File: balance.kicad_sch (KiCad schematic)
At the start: 30 parts, among them Q10 2N7002, Q5 AO3401A, Q6 AO3401A, Q7 AO3401A, Q8 2N7002, Q9 2N7002

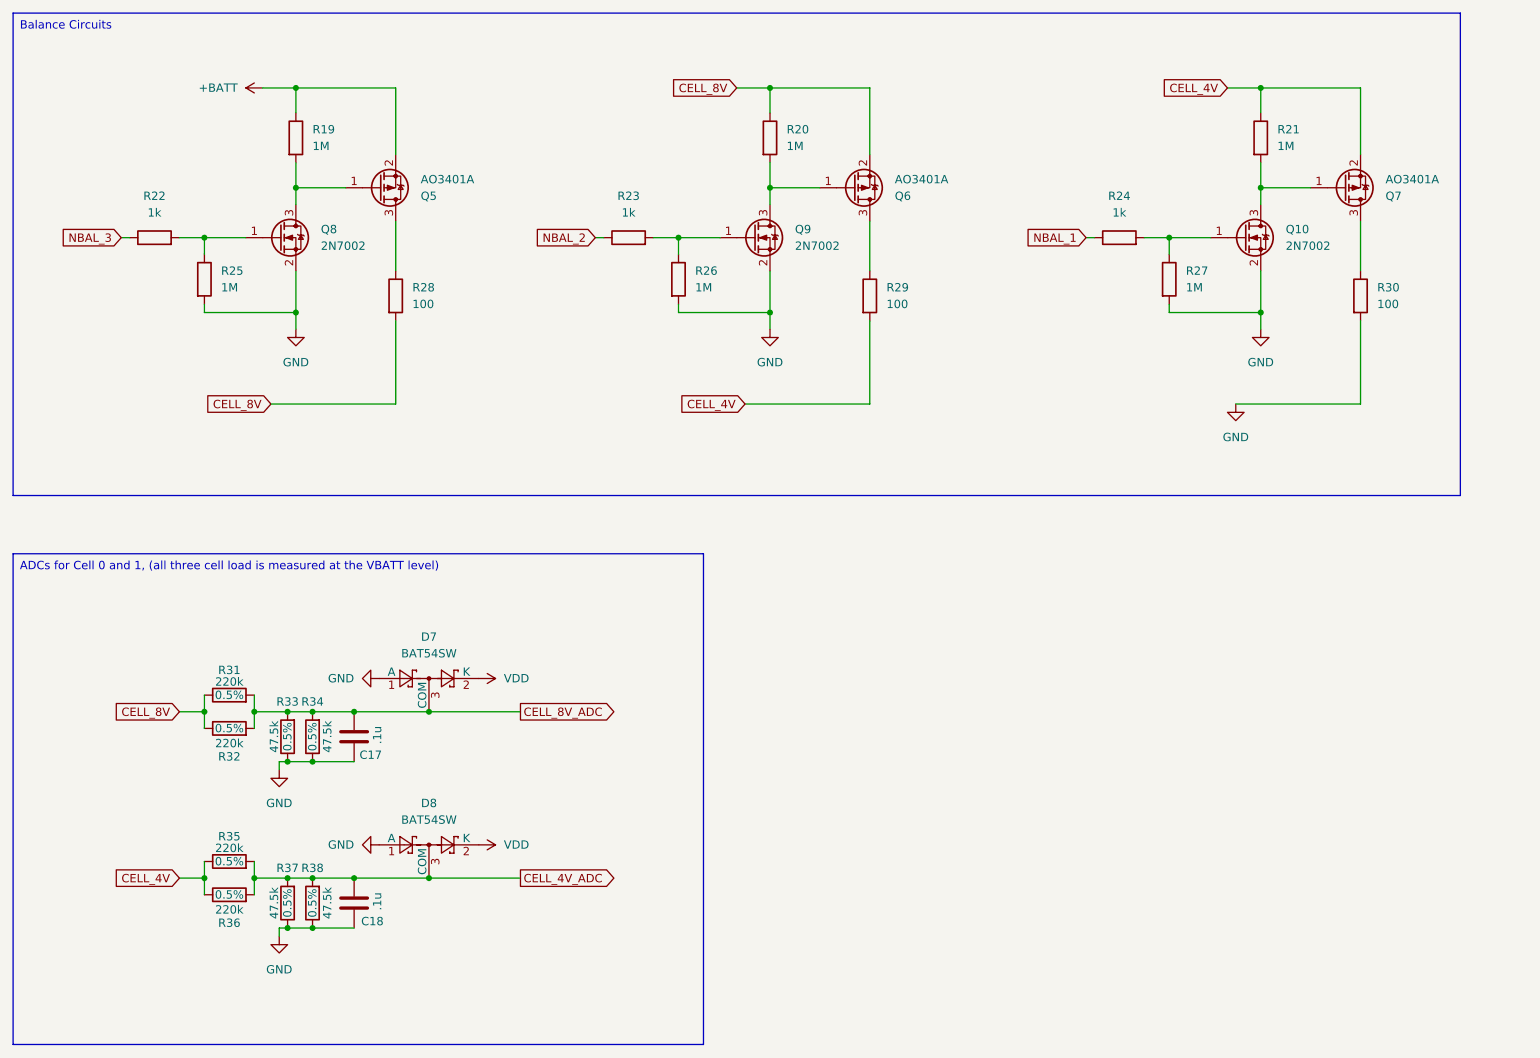
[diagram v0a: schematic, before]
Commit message: Adding flow chart to main.c Adding leds on balancers
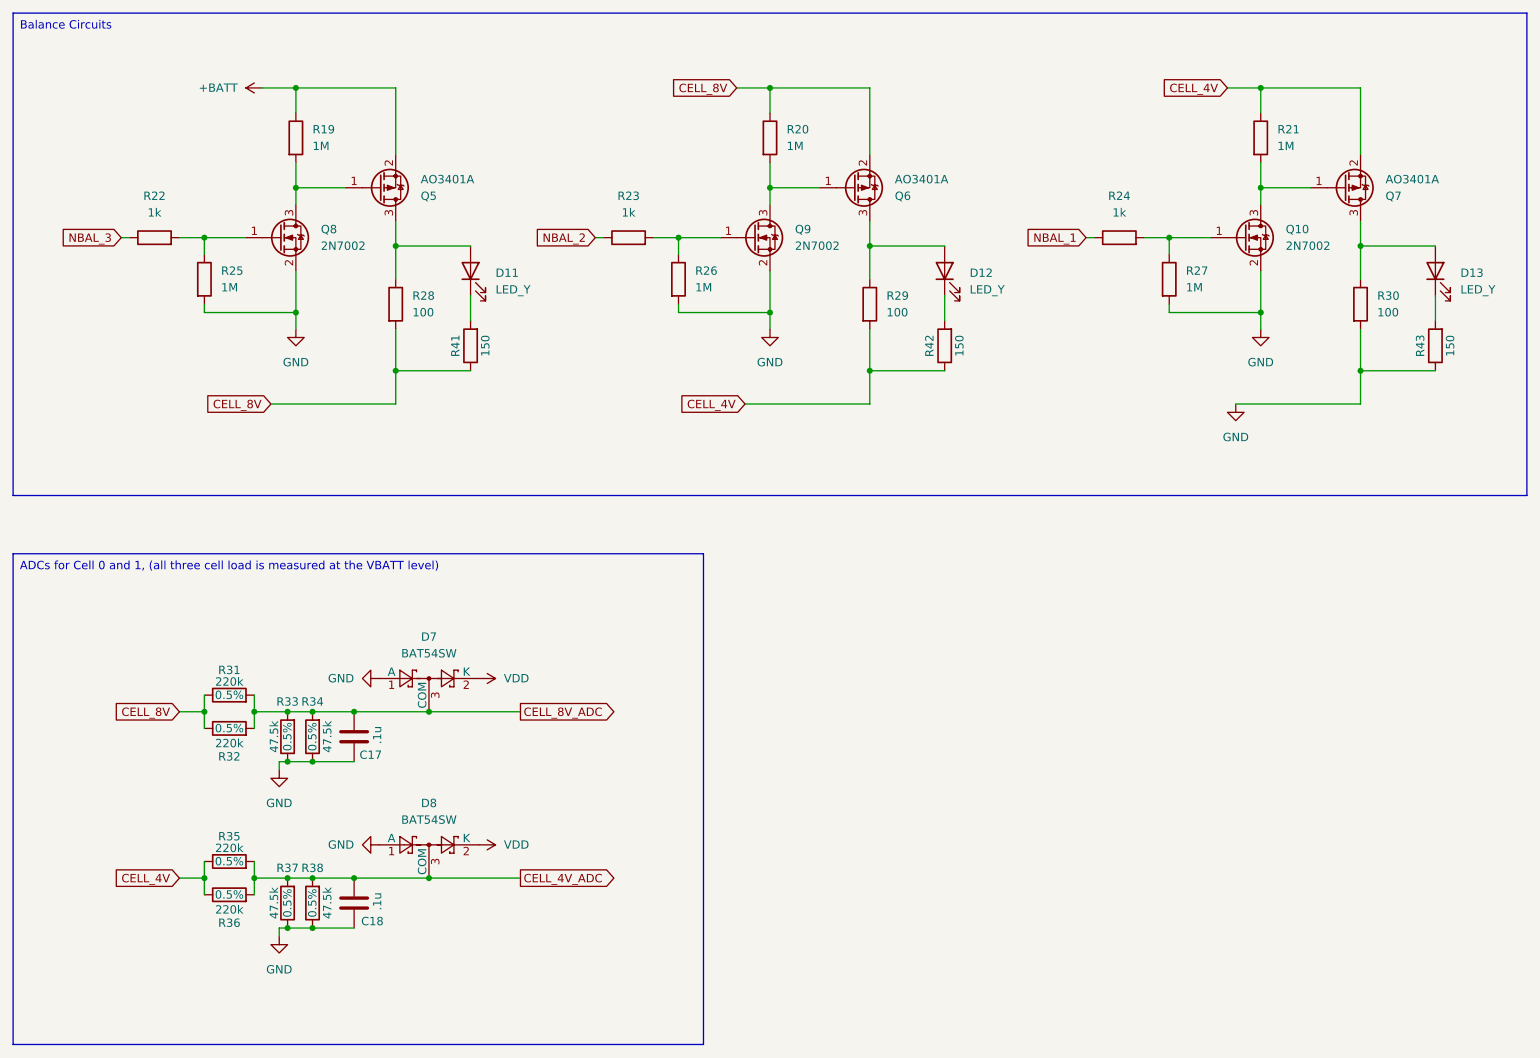
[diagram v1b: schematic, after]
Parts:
- added D11, D12, D13: LED_Y, LED_SMD:LED_0603_1608Metric, symbol Device:LED
- added R41, R42, R43: 150, Resistor_SMD:R_0402_1005Metric, symbol Device:R
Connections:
- net CELL_4V: now also R42.1
- net CELL_8V: now also R41.1
- net GND: now also R43.1
- net at Q7.3 (D), R30.1: now also D13.2 (A)
- net at Q6.3 (D), R29.1: now also D12.2 (A)
- net at Q5.3 (D), R28.1: now also D11.2 (A)
- new net: D12.1 (K), R42.2
- new net: D13.1 (K), R43.2
- new net: D11.1 (K), R41.2
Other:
- moved on the sheet: R28, R29, R30

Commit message: Starting draft of ADC multiplexer
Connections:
- net CELL_4V: no longer R35.1, R36.1
- net CELL_8V: no longer R31.1, R32.1
- net CELL_4V_ADC: no longer names the net of C18.1, D8.3 (COM), R35.2, R36.2, R37.2, R38.2
- net CELL_8V_ADC: no longer names the net of C17.1, D7.3 (COM), R31.2, R32.2, R33.2, R34.2
- new net: R31.1, R32.1
- new net: R35.1, R36.1
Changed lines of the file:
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@@
-		)
-	)
-	(global_label "CELL_4V"
-		(shape input)
-		(at 63.5 157.48 180)
-		(fields_autoplaced yes)
-		(effects
-			(font
-				(size 1.27 1.27)
-			)
-			(justify right)
-		)
-		(property "Intersheetrefs" "${INTERSHEET_REFS}"
-			(at 52.7739 157.48 0)
-			(effects
-				(font
-					(size 1.27 1.27)
-				)
-				(justify right)
-				(hide yes)
-			)
 		)
 	)
@@
 				)
 				(justify right)
-				(hide yes)
-			)
-		)
-	)
-	(global_label "CELL_4V_ADC"
-		(shape output)
-		(at 115.57 157.48 0)
-		(fields_autoplaced yes)
-		(effects
-			(font
-				(size 1.27 1.27)
-			)
-			(justify left)
-		)
-		(property "Intersheetrefs" "${INTERSHEET_REFS}"
-			(at 130.8923 157.48 0)
-			(effects
-				(font
-					(size 1.27 1.27)
-				)
-				(justify left)
 				(hide yes)
 			)
@@
 				(hide yes)
 			)
-		)
-	)
-	(global_label "CELL_8V"
-		(shape input)
-		(at 63.5 132.08 180)
-		(fields_autoplaced yes)
-		(effects
-			(font
-				(size 1.27 1.27)
-			)
-			(justify right)
-		)
-		(property "Intersheetrefs" "${INTERSHEET_REFS}"
-			(at 52.7739 132.08 0)
-			(effects
-				(font
-					(size 1.27 1.27)
-				)
-				(justify right)
-				(hide yes)
-			)
-		)
-	)
-	(global_label "CELL_8V_ADC"
-		(shape output)
-		(at 115.57 132.08 0)
-		(fields_autoplaced yes)
-		(effects
-			(font
-				(size 1.27 1.27)
-			)
-			(justify left)
-		)
-		(property "Intersheetrefs" "${INTERSHEET_REFS}"
-			(at 130.8923 132.08 0)
-			(effects
-				(font
-					(size 1.27 1.27)
-				)
-				(justify left)
-				(hide yes)
-			)

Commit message: Adding ADC multiplexer, protection diodes
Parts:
- removed C17, C18: .1u, Capacitor_SMD:C_0603_1608Metric, symbol Device:C
- removed D7, D8: BAT54SW, Package_TO_SOT_SMD:SOT-323_SC-70, symbol Diode:BAT54SW
- removed R31, R32, R35, R36: 220k, Resistor_SMD:R_0402_1005Metric, symbol Device:R
- removed R33, R34, R37, R38: 47.5k, Resistor_SMD:R_0402_1005Metric, symbol Device:R

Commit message: Decent pass
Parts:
- renumbered D11 to D13, D12 to D14, D13 to D15, Q6 to Q10, Q10 to Q11, Q7 to Q12, Q8 to Q7, Q5 to Q8, R22 to R25, R25 to R26, R19 to R27, R41 to R29, R23 to R30, R26 to R31, R20 to R32, R29 to R33, R42 to R34, R24 to R35, R27 to R36, R21 to R37, R30 to R38, R43 to R39
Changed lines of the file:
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@@
 		(dnp no)
 		(fields_autoplaced yes)
-		(property "Reference" "D12"
+		(property "Reference" "D14"
 			(at 184.15 65.0874 90)
 			(effects
@@
 			(project "JPBms2"
 				(path "/d86e471c-a8be-422d-a5d1-5a4699b7b766/220685a5-608c-4c12-9441-6825efcef07c"
-					(reference "D12")
+					(reference "D14")
 					(unit 1)
 				)
@@
 		(dnp no)
 		(fields_autoplaced yes)
-		(property "Reference" "#PWR042"
+		(property "Reference" "#PWR048"
 			(at 80.01 36.83 0)
 			(effects
@@
 			(project "JPBms2"
 				(path "/d86e471c-a8be-422d-a5d1-5a4699b7b766/220685a5-608c-4c12-9441-6825efcef07c"
-					(reference "#PWR042")
+					(reference "#PWR048")
 					(unit 1)
 				)
@@
 		(dnp no)
 		(fields_autoplaced yes)
-		(property "Reference" "R25"
+		(property "Reference" "R26"
 			(at 69.85 64.7699 0)
 			(effects
@@
 			(project "JPBms2"
 				(path "/d86e471c-a8be-422d-a5d1-5a4699b7b766/220685a5-608c-4c12-9441-6825efcef07c"
-					(reference "R25")
+					(reference "R26")
 					(unit 1)
 				)
@@
 		(dnp no)
 		(fields_autoplaced yes)
-		(property "Reference" "R27"
+		(property "Reference" "R36"
 			(at 217.17 64.7699 0)
 			(effects
@@
 			(project "JPBms2"
 				(path "/d86e471c-a8be-422d-a5d1-5a4699b7b766/220685a5-608c-4c12-9441-6825efcef07c"
-					(reference "R27")
+					(reference "R36")
 					(unit 1)
 				)
@@
 		(dnp no)
 		(fields_autoplaced yes)
-		(property "Reference" "R24"
+		(property "Reference" "R35"
 			(at 207.01 53.34 90)
 			(effects
@@
 			(project "JPBms2"
 				(path "/d86e471c-a8be-422d-a5d1-5a4699b7b766/220685a5-608c-4c12-9441-6825efcef07c"
-					(reference "R24")
+					(reference "R35")
 					(unit 1)
 				)
@@
 		(on_board yes)
 		(dnp no)
-		(property "Reference" "R42"
+		(property "Reference" "R34"
 			(at 178.054 76.2 90)
 			(effects
@@
 			(project "JPBms2"
 				(path "/d86e471c-a8be-422d-a5d1-5a4699b7b766/220685a5-608c-4c12-9441-6825efcef07c"
-					(reference "R42")
+					(reference "R34")
 					(unit 1)
 				)
@@
 		(on_board yes)
 		(dnp no)
-		(property "Reference" "R43"
+		(property "Reference" "R39"
 			(at 252.984 76.2 90)
 			(effects
@@
 			(project "JPBms2"
 				(path "/d86e471c-a8be-422d-a5d1-5a4699b7b766/220685a5-608c-4c12-9441-6825efcef07c"
-					(reference "R43")
+					(reference "R39")
 					(unit 1)
 				)
@@
 		(dnp no)
 		(fields_autoplaced yes)
-		(property "Reference" "Q8"
+		(property "Reference" "Q7"
 			(at 85.09 58.4199 0)
 			(effects
@@
 			(project "JPBms2"
 				(path "/d86e471c-a8be-422d-a5d1-5a4699b7b766/220685a5-608c-4c12-9441-6825efcef07c"
-					(reference "Q8")
+					(reference "Q7")
 					(unit 1)
 				)
@@
 		(dnp no)
 		(fields_autoplaced yes)
-		(property "Reference" "R26"
+		(property "Reference" "R31"
 			(at 142.24 64.7699 0)
 			(effects
@@
 			(project "JPBms2"
 				(path "/d86e471c-a8be-422d-a5d1-5a4699b7b766/220685a5-608c-4c12-9441-6825efcef07c"
-					(reference "R26")
+					(reference "R31")
 					(unit 1)
 				)
@@
 		(on_board yes)
 		(dnp no)
-		(property "Reference" "R41"
+		(property "Reference" "R29"
 			(at 105.664 76.2 90)
 			(effects
@@
 			(project "JPBms2"
 				(path "/d86e471c-a8be-422d-a5d1-5a4699b7b766/220685a5-608c-4c12-9441-6825efcef07c"
-					(reference "R41")
+					(reference "R29")
 					(unit 1)
 				)
@@
 		(dnp no)
 		(fields_autoplaced yes)
-		(property "Reference" "R20"
+		(property "Reference" "R32"
 			(at 156.21 43.1799 0)
 			(effects
@@
 			(project "JPBms2"
 				(path "/d86e471c-a8be-422d-a5d1-5a4699b7b766/220685a5-608c-4c12-9441-6825efcef07c"
-					(reference "R20")
+					(reference "R32")
 					(unit 1)
 				)
@@
 		(dnp no)
 		(fields_autoplaced yes)
-		(property "Reference" "#PWR046"
+		(property "Reference" "#PWR051"
 			(at 224.79 91.44 0)
 			(effects
@@
 			(project "JPBms2"
 				(path "/d86e471c-a8be-422d-a5d1-5a4699b7b766/220685a5-608c-4c12-9441-6825efcef07c"
-					(reference "#PWR046")
+					(reference "#PWR051")
 					(unit 1)
 				)
@@
 		(dnp no)
 		(fields_autoplaced yes)
-		(property "Reference" "Q10"
+		(property "Reference" "Q11"
 			(at 232.41 58.4199 0)
 			(effects
@@
 			(project "JPBms2"
 				(path "/d86e471c-a8be-422d-a5d1-5a4699b7b766/220685a5-608c-4c12-9441-6825efcef07c"
-					(reference "Q10")
+					(reference "Q11")
 					(unit 1)
 				)
@@
 		(dnp no)
 		(fields_autoplaced yes)
-		(property "Reference" "R30"
+		(property "Reference" "R38"
 			(at 246.38 68.5799 0)
 			(effects
@@
 			(project "JPBms2"
 				(path "/d86e471c-a8be-422d-a5d1-5a4699b7b766/220685a5-608c-4c12-9441-6825efcef07c"
-					(reference "R30")
+					(reference "R38")
 					(unit 1)
 				)
@@
 		(dnp no)
 		(fields_autoplaced yes)
-		(property "Reference" "#PWR045"
+		(property "Reference" "#PWR052"
 			(at 228.6 80.01 0)
 			(effects
@@
 			(project "JPBms2"
 				(path "/d86e471c-a8be-422d-a5d1-5a4699b7b766/220685a5-608c-4c12-9441-6825efcef07c"
-					(reference "#PWR045")
+					(reference "#PWR052")
 					(unit 1)
 				)
@@
 		(dnp no)
 		(fields_autoplaced yes)
-		(property "Reference" "R19"
+		(property "Reference" "R27"
 			(at 83.82 43.1799 0)
 			(effects
@@
 			(project "JPBms2"
 				(path "/d86e471c-a8be-422d-a5d1-5a4699b7b766/220685a5-608c-4c12-9441-6825efcef07c"
-					(reference "R19")
+					(reference "R27")
 					(unit 1)
 				)
@@
 		(dnp no)
 		(fields_autoplaced yes)
-		(property "Reference" "R23"
+		(property "Reference" "R30"
 			(at 132.08 53.34 90)
 			(effects
@@
 			(project "JPBms2"
 				(path "/d86e471c-a8be-422d-a5d1-5a4699b7b766/220685a5-608c-4c12-9441-6825efcef07c"
-					(reference "R23")
+					(reference "R30")
 					(unit 1)
 				)
@@
 		(dnp no)
 		(fields_autoplaced yes)
-		(property "Reference" "D11"
+		(property "Reference" "D13"
 			(at 111.76 65.0874 90)
 			(effects
@@
 			(project "JPBms2"
 				(path "/d86e471c-a8be-422d-a5d1-5a4699b7b766/220685a5-608c-4c12-9441-6825efcef07c"
-					(reference "D11")
+					(reference "D13")
 					(unit 1)
 				)
@@
 		(dnp no)
 		(fields_autoplaced yes)
-		(property "Reference" "R22"
+		(property "Reference" "R25"
 			(at 59.69 53.34 90)
 			(effects
@@
 			(project "JPBms2"
 				(path "/d86e471c-a8be-422d-a5d1-5a4699b7b766/220685a5-608c-4c12-9441-6825efcef07c"
-					(reference "R22")
+					(reference "R25")
 					(unit 1)
 				)
@@
 		(dnp no)
 		(fields_autoplaced yes)
-		(property "Reference" "R29"
+		(property "Reference" "R33"
 			(at 171.45 68.5799 0)
 			(effects
@@
 			(project "JPBms2"
 				(path "/d86e471c-a8be-422d-a5d1-5a4699b7b766/220685a5-608c-4c12-9441-6825efcef07c"
-					(reference "R29")
+					(reference "R33")
 					(unit 1)
 				)
@@
 		(on_board yes)
 		(dnp no)
-		(property "Reference" "Q5"
+		(property "Reference" "Q8"
 			(at 100.33 53.3401 0)
 			(effects
@@
 			(project "JPBms2"
 				(path "/d86e471c-a8be-422d-a5d1-5a4699b7b766/220685a5-608c-4c12-9441-6825efcef07c"
-					(reference "Q5")
+					(reference "Q8")
 					(unit 1)
 				)
@@
 		(on_board yes)
 		(dnp no)
-		(property "Reference" "Q6"
+		(property "Reference" "Q10"
 			(at 172.72 53.3401 0)
 			(effects
@@
 			(project "JPBms2"
 				(path "/d86e471c-a8be-422d-a5d1-5a4699b7b766/220685a5-608c-4c12-9441-6825efcef07c"
-					(reference "Q6")
+					(reference "Q10")
 					(unit 1)
 				)
@@
 		(dnp no)
 		(fields_autoplaced yes)
-		(property "Reference" "#PWR043"
+		(property "Reference" "#PWR049"
 			(at 81.28 80.01 0)
 			(effects
@@
 			(project "JPBms2"
 				(path "/d86e471c-a8be-422d-a5d1-5a4699b7b766/220685a5-608c-4c12-9441-6825efcef07c"
-					(reference "#PWR043")
+					(reference "#PWR049")
 					(unit 1)
 				)
@@
 		(on_board yes)
 		(dnp no)
-		(property "Reference" "Q7"
+		(property "Reference" "Q12"
 			(at 247.65 53.3401 0)
 			(effects
@@
 			(project "JPBms2"
 				(path "/d86e471c-a8be-422d-a5d1-5a4699b7b766/220685a5-608c-4c12-9441-6825efcef07c"
-					(reference "Q7")
+					(reference "Q12")
 					(unit 1)
 				)
@@
 		(dnp no)
 		(fields_autoplaced yes)
-		(property "Reference" "#PWR044"
+		(property "Reference" "#PWR050"
 			(at 153.67 80.01 0)
 			(effects
@@
 			(project "JPBms2"
 				(path "/d86e471c-a8be-422d-a5d1-5a4699b7b766/220685a5-608c-4c12-9441-6825efcef07c"
-					(reference "#PWR044")
+					(reference "#PWR050")
 					(unit 1)
 				)
@@
 		(dnp no)
 		(fields_autoplaced yes)
-		(property "Reference" "D13"
+		(property "Reference" "D15"
 			(at 259.08 65.0874 90)
 			(effects
@@
 			(project "JPBms2"
 				(path "/d86e471c-a8be-422d-a5d1-5a4699b7b766/220685a5-608c-4c12-9441-6825efcef07c"
-					(reference "D13")
+					(reference "D15")
 					(unit 1)
 				)
@@
 		(dnp no)
 		(fields_autoplaced yes)
-		(property "Reference" "R21"
+		(property "Reference" "R37"
 			(at 231.14 43.1799 0)
 			(effects
@@
 			(project "JPBms2"
 				(path "/d86e471c-a8be-422d-a5d1-5a4699b7b766/220685a5-608c-4c12-9441-6825efcef07c"
-					(reference "R21")
-					(unit 1)
-				)
+					(reference "R37")
+					(unit 1)
+				)
